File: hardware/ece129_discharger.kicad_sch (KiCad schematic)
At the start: 0 parts

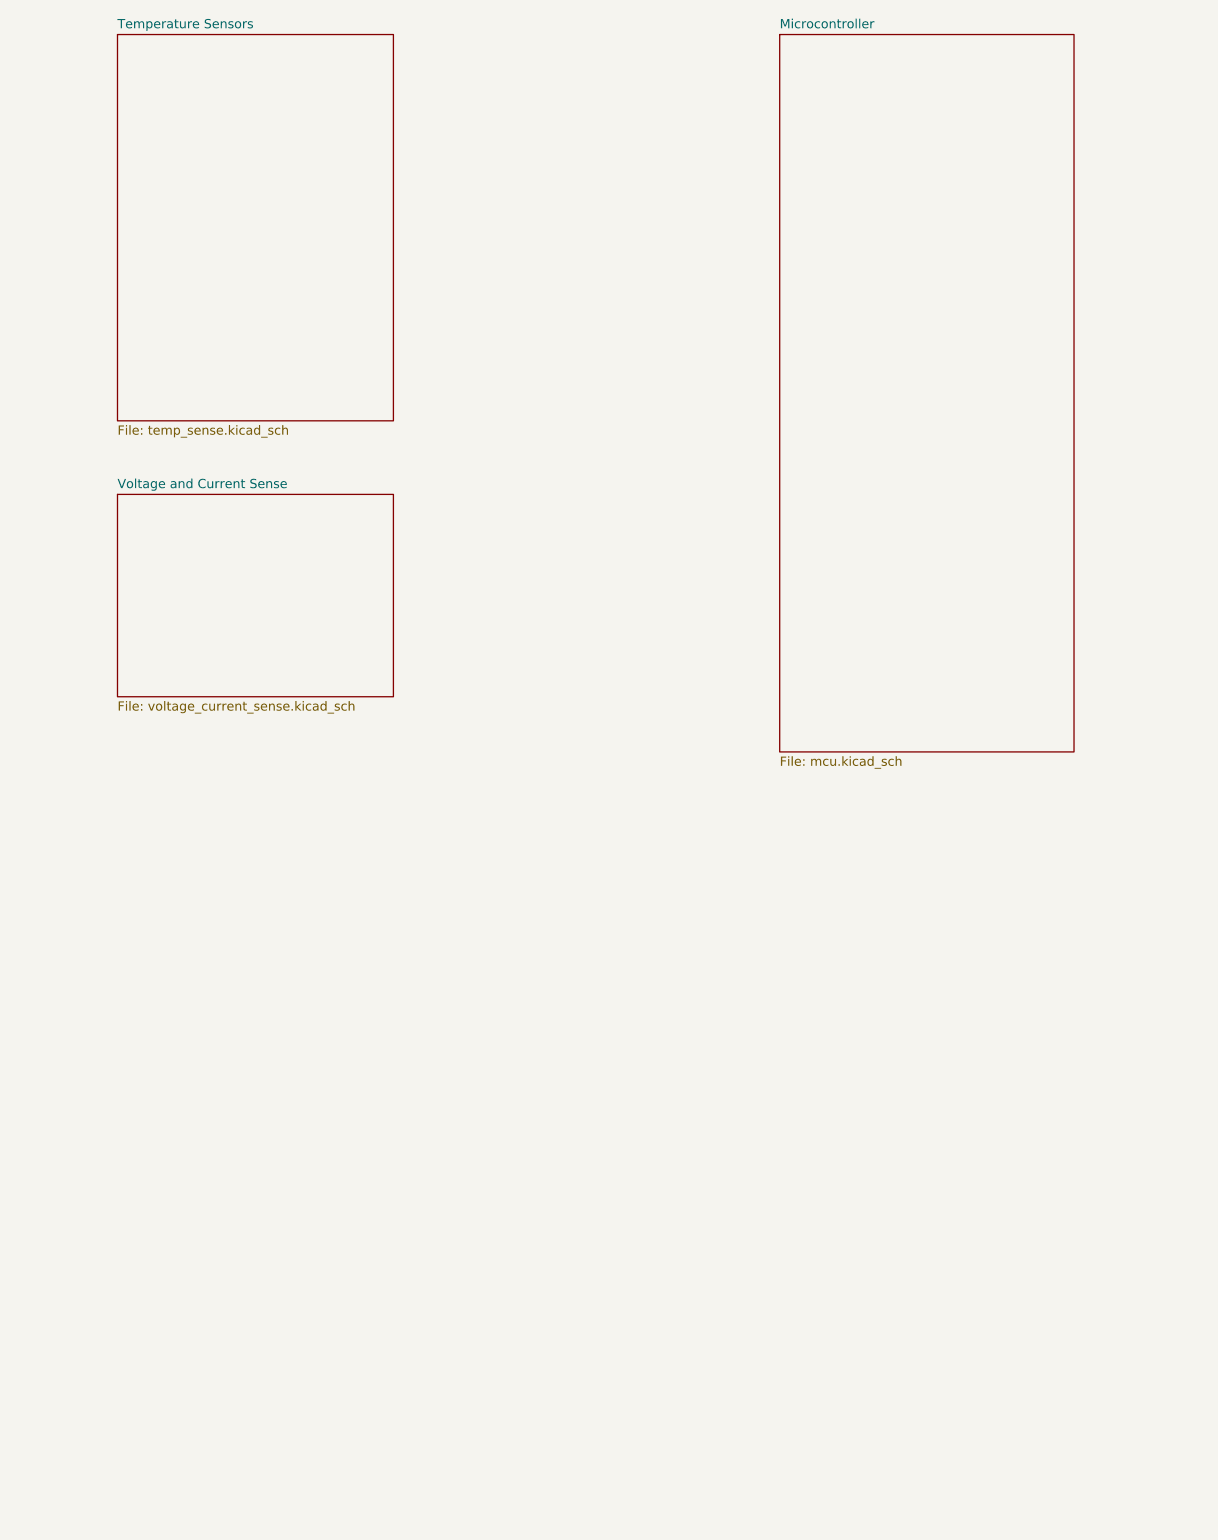
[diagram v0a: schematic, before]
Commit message: MBR0.0.1 - Begin addition of sheet pins to MCU page
Incomplete
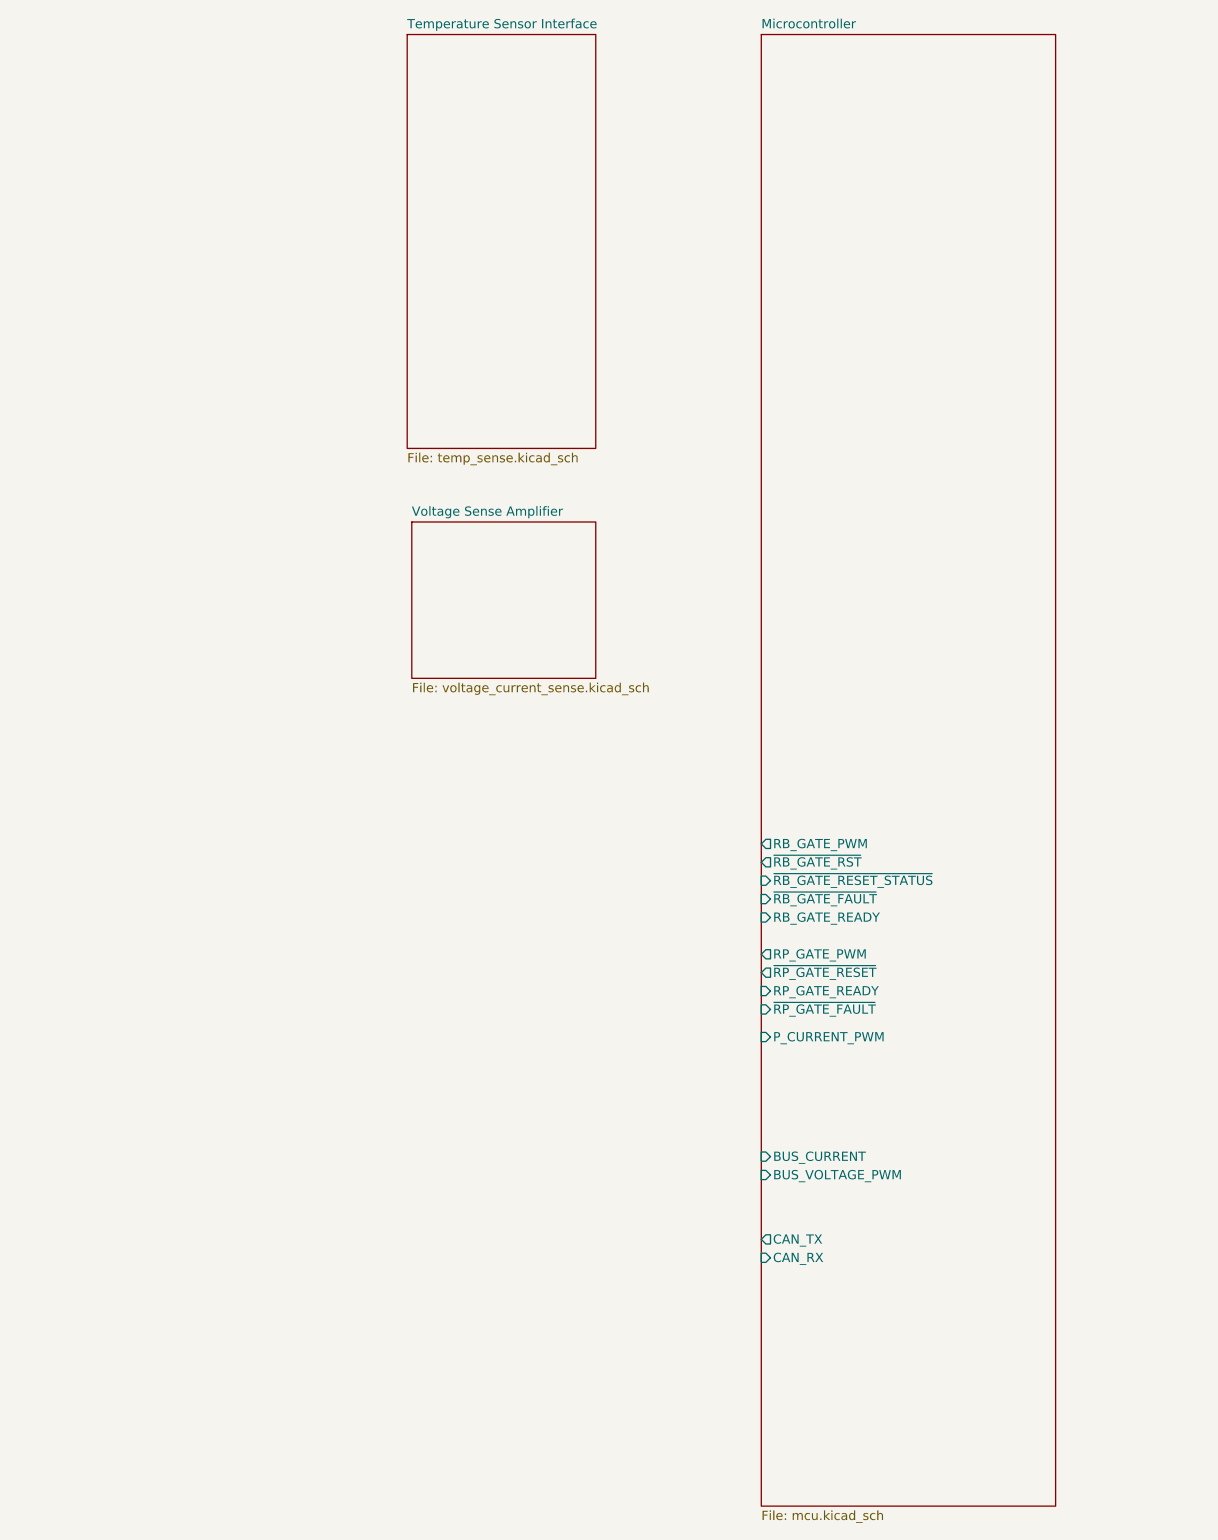
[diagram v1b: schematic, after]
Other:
- sheet Temperature Sensors renamed Temperature Sensor Interface
- sheet Voltage and Current Sense renamed Voltage Sense Amplifier
- sheet Microcontroller ports: added BUS_CURRENT, BUS_VOLTAGE_PWM, CAN_RX, CAN_TX, P_CURRENT_PWM, RB_GATE_PWM, RB_GATE_READY, RP_GATE_PWM, RP_GATE_READY, ~{RB_GATE_FAULT}, ~{RB_GATE_RESET_STATUS}, ~{RB_GATE_RST}, ~{RP_GATE_FAULT}, ~{RP_GATE_RESET}; removed none
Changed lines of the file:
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@@
 	)
 	(sheet
-		(at 152.4 50.8)
-		(size 40.64 99.06)
+		(at 149.86 50.8)
+		(size 40.64 203.2)
 		(exclude_from_sim no)
 		(in_bom yes)
@@
 		)
 		(property "Sheetname" "Microcontroller"
-			(at 152.4 50.0884 0)
+			(at 149.86 50.0884 0)
 			(show_name no)
 			(do_not_autoplace no)
@@
 		)
 		(property "Sheetfile" "mcu.kicad_sch"
-			(at 152.4 150.4446 0)
+			(at 149.86 254.5846 0)
 			(show_name no)
 			(do_not_autoplace no)
@@
 				)
 				(justify left top)
+			)
+		)
+		(pin "~{RB_GATE_RST}" output
+			(at 149.86 165.1 180)
+			(effects
+				(font
+					(size 1.27 1.27)
+				)
+				(justify left)
+			)
+		)
+		(pin "~{RB_GATE_FAULT}" input
+			(at 149.86 170.18 180)
+			(effects
+				(font
+					(size 1.27 1.27)
+				)
+				(justify left)
+			)
+		)
+		(pin "RB_GATE_READY" input
+			(at 149.86 172.72 180)
+			(effects
+				(font
+					(size 1.27 1.27)
+				)
+				(justify left)
+			)
+		)
+		(pin "~{RB_GATE_RESET_STATUS}" input
+			(at 149.86 167.64 180)
+			(effects
+				(font
+					(size 1.27 1.27)
+				)
+				(justify left)
+			)
+		)
+		(pin "RB_GATE_PWM" output
+			(at 149.86 162.56 180)
+			(effects
+				(font
+					(size 1.27 1.27)
+				)
+				(justify left)
+			)
+		)
+		(pin "RP_GATE_PWM" output
+			(at 149.86 177.8 180)
+			(effects
+				(font
+					(size 1.27 1.27)
+				)
+				(justify left)
+			)
+		)
+		(pin "RP_GATE_READY" input
+			(at 149.86 182.88 180)
+			(effects
+				(font
+					(size 1.27 1.27)
+				)
+				(justify left)
+			)
+		)
+		(pin "~{RP_GATE_RESET}" output
+			(at 149.86 180.34 180)
+			(effects
+				(font
+					(size 1.27 1.27)
+				)
+				(justify left)
+			)
+		)
+		(pin "~{RP_GATE_FAULT}" input
+			(at 149.86 185.42 180)
+			(effects
+				(font
+					(size 1.27 1.27)
+				)
+				(justify left)
+			)
+		)
+		(pin "BUS_CURRENT" input
+			(at 149.86 205.74 180)
+			(effects
+				(font
+					(size 1.27 1.27)
+				)
+				(justify left)
+			)
+		)
+		(pin "BUS_VOLTAGE_PWM" input
+			(at 149.86 208.28 180)
+			(effects
+				(font
+					(size 1.27 1.27)
+				)
+				(justify left)
+			)
+		)
+		(pin "CAN_RX" input
+			(at 149.86 219.71 180)
+			(effects
+				(font
+					(size 1.27 1.27)
+				)
+				(justify left)
+			)
+		)
+		(pin "CAN_TX" output
+			(at 149.86 217.17 180)
+			(effects
+				(font
+					(size 1.27 1.27)
+				)
+				(justify left)
+			)
+		)
+		(pin "P_CURRENT_PWM" input
+			(at 149.86 189.23 180)
+			(effects
+				(font
+					(size 1.27 1.27)
+				)
+				(justify left)
 			)
 		)
@@
 	)
 	(sheet
-		(at 60.96 50.8)
-		(size 38.1 53.34)
+		(at 100.965 50.8)
+		(size 26.035 57.15)
 		(exclude_from_sim no)
 		(in_bom yes)
@@
 			(color 0 0 0 0)
 		)
-		(property "Sheetname" "Temperature Sensors"
-			(at 60.96 50.0884 0)
+		(property "Sheetname" "Temperature Sensor Interface"
+			(at 100.965 50.0884 0)
 			(show_name no)
 			(do_not_autoplace no)
@@
 		)
 		(property "Sheetfile" "temp_sense.kicad_sch"
-			(at 60.96 104.7246 0)
+			(at 100.965 108.5346 0)
 			(show_name no)
 			(do_not_autoplace no)
@@
 	)
 	(sheet
-		(at 60.96 114.3)
-		(size 38.1 27.94)
+		(at 101.6 118.11)
+		(size 25.4 21.59)
 		(exclude_from_sim no)
 		(in_bom yes)
@@
 			(color 0 0 0 0)
 		)
-		(property "Sheetname" "Voltage and Current Sense"
-			(at 60.96 113.5884 0)
+		(property "Sheetname" "Voltage Sense Amplifier"
+			(at 101.6 117.3984 0)
 			(show_name no)
 			(do_not_autoplace no)
@@
 		)
 		(property "Sheetfile" "voltage_current_sense.kicad_sch"
-			(at 60.96 142.8246 0)
-			(show_name no)
-			(do_not_autoplace no)
+			(at 101.6 140.2846 0)
+			(show_name no)
+			(do_not_autoplace no)

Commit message: R0.0.2 Add more connections to MCU, some connectors
commit d1f92fde9a9b01f608e388bb27e003f4547c4ba5
Author: fezboy <31973884+fezboy@users.noreply.github.com>
Date:   Tue Apr 28 12:29:51 2026 -0700

    R0.0.2 Add more connections to MCU, some connectors
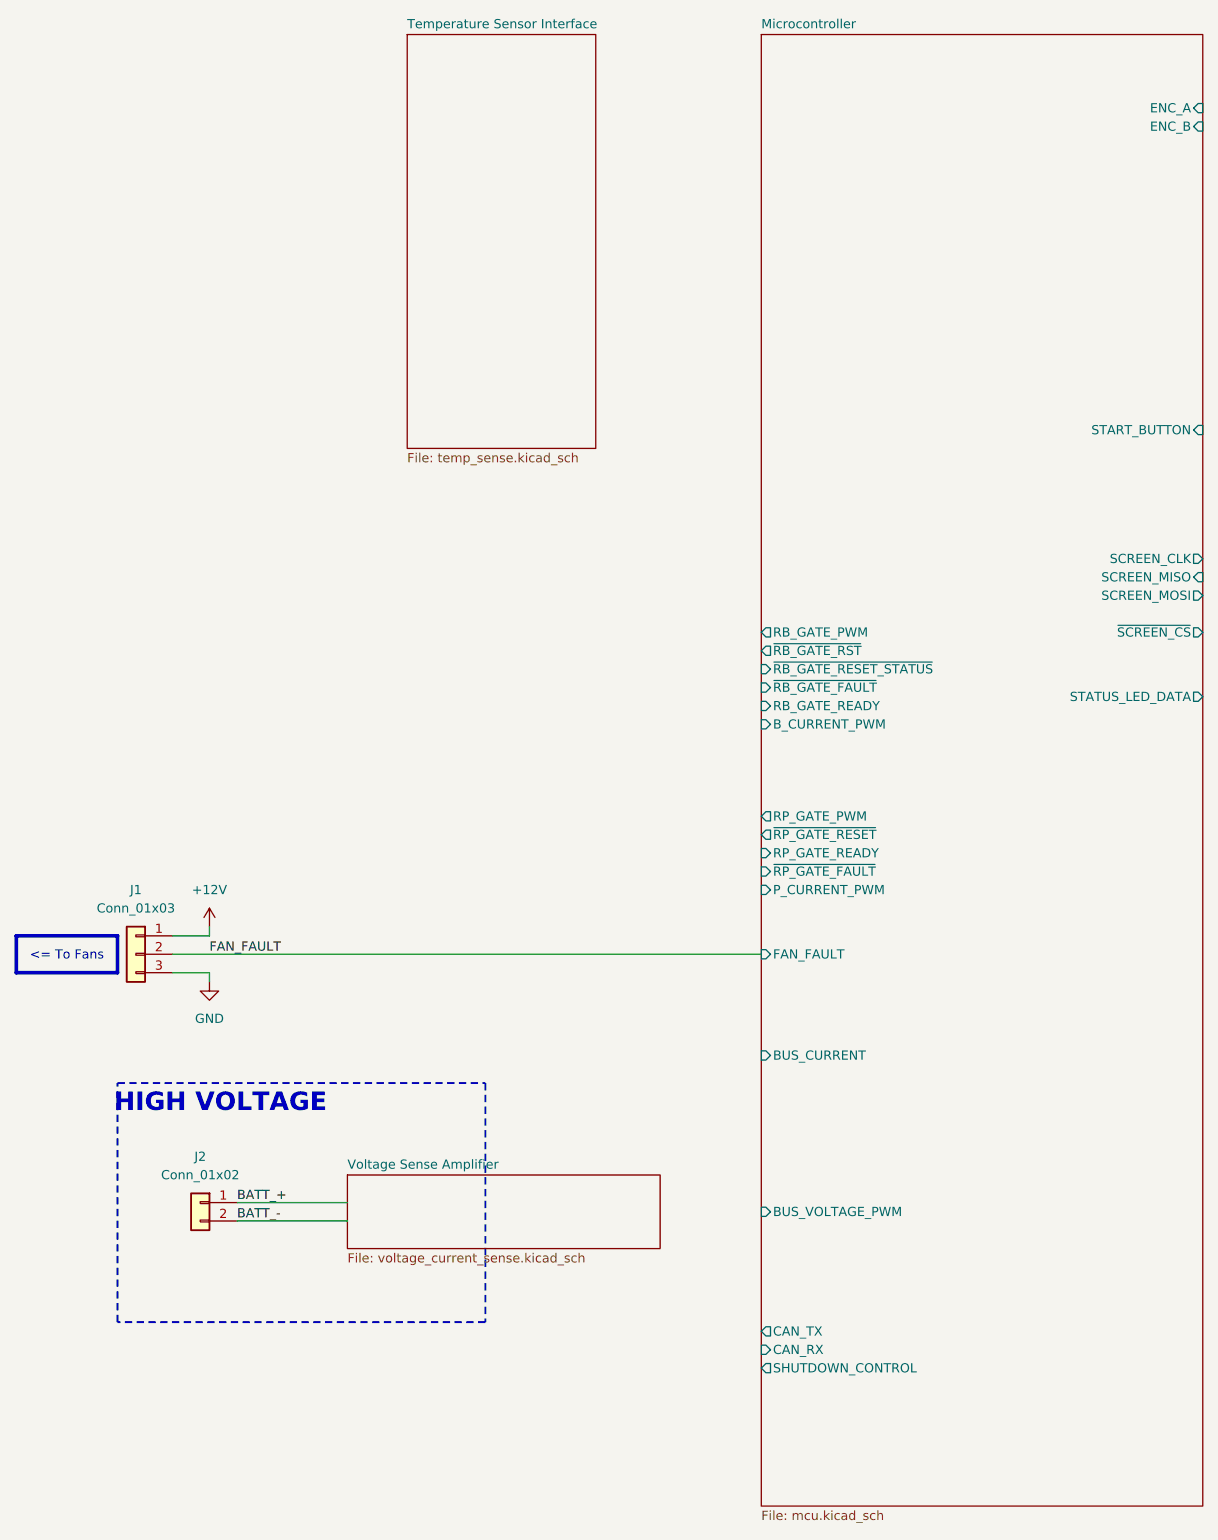
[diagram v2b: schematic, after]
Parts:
- added J1: Conn_01x03, symbol Connector_Generic:Conn_01x03
- added J2: Conn_01x02, symbol Connector_Generic:Conn_01x02
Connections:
- new net +12V: J1.1 (Pin_1)
- new net BATT_+: J2.1 (Pin_1)
- new net BATT_-: J2.2 (Pin_2)
- new net FAN_FAULT: J1.2 (Pin_2)
- new net GND: J1.3 (Pin_3)
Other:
- sheet Microcontroller ports: added B_CURRENT_PWM, ENC_A, ENC_B, FAN_FAULT, SCREEN_CLK, SCREEN_MISO, SCREEN_MOSI, SHUTDOWN_CONTROL, START_BUTTON, STATUS_LED_DATA, ~{SCREEN_CS}; removed none
- note added: "HIGH VOLTAGE"
- title: [BOARD NAME] -> Discharger Main Board

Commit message: adding connectors
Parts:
- added J10, J11, J3, J4, J5, J6, J7, J8, J9: Conn_01x02, symbol Connector_Generic:Conn_01x02
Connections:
- new net CurrentSens_Out: J11.1 (Pin_1)
- new net CurrentSens_Vref: J11.2 (Pin_2)
- new net Temp1_1: J3.1 (Pin_1)
- new net Temp1_2: J3.2 (Pin_2)
- new net Temp2_1: J4.1 (Pin_1)
- new net Temp2_2: J4.2 (Pin_2)
- new net Temp3_1: J5.1 (Pin_1)
- new net Temp3_2: J5.2 (Pin_2)
- new net Temp4_1: J6.1 (Pin_1)
- new net Temp4_2: J6.2 (Pin_2)
- new net Temp5_1: J7.1 (Pin_1)
- new net Temp5_2: J7.2 (Pin_2)
- new net Temp6_1: J8.1 (Pin_1)
- new net Temp6_2: J8.2 (Pin_2)
- new net Temp7_1: J9.1 (Pin_1)
- new net Temp7_2: J9.2 (Pin_2)
- new net Temp8_1: J10.1 (Pin_1)
- new net Temp8_2: J10.2 (Pin_2)

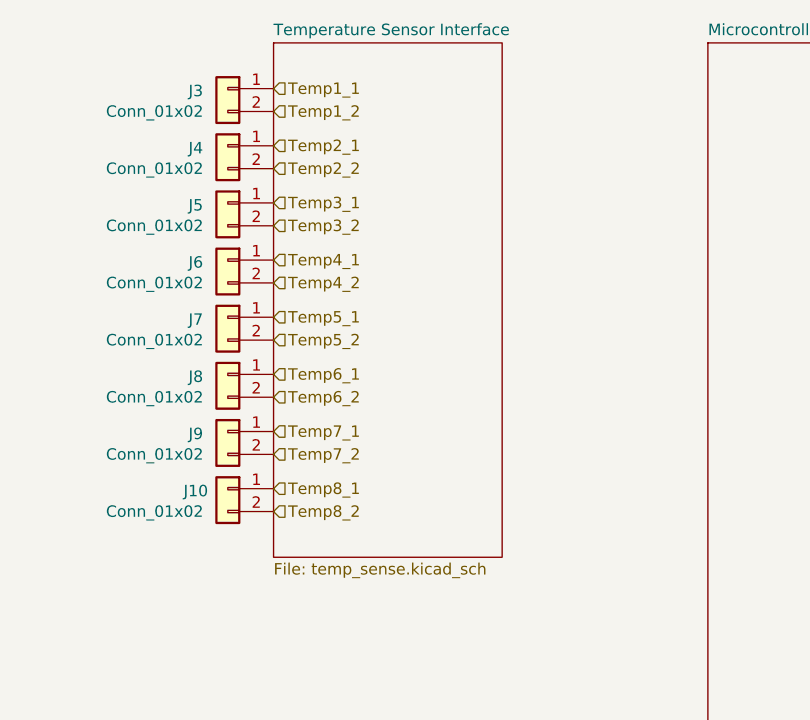
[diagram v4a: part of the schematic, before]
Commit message: Pin assignment first draft
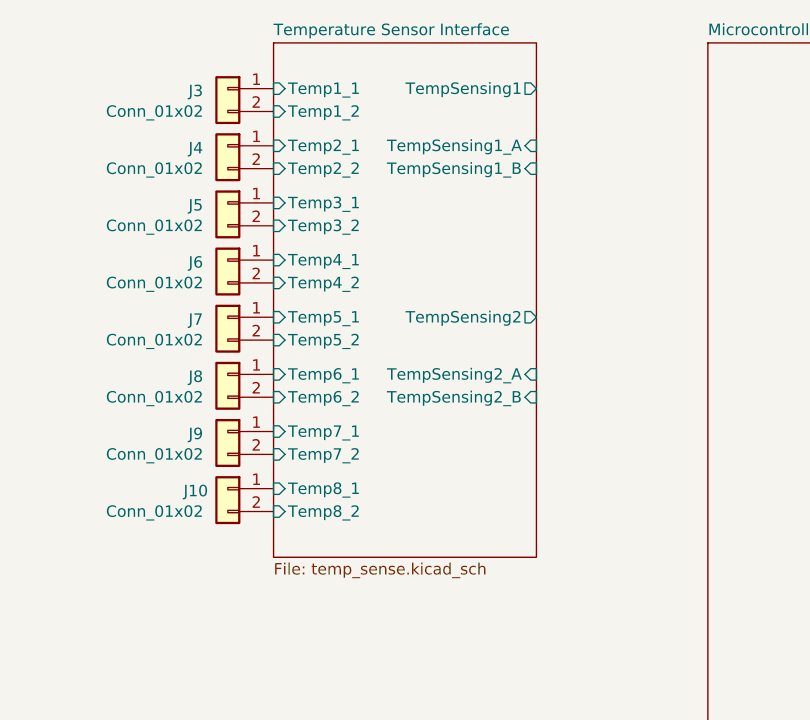
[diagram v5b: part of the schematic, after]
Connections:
- net Temp1_1 renamed Temperature Sensor Interface/Temp1_1
- net Temp1_2 renamed Temperature Sensor Interface/Temp1_2
- net Temp2_1 renamed Temperature Sensor Interface/Temp2_1
- net Temp2_2 renamed Temperature Sensor Interface/Temp2_2
- net Temp3_1 renamed Temperature Sensor Interface/Temp3_1
- net Temp3_2 renamed Temperature Sensor Interface/Temp3_2
- net Temp4_1 renamed Temperature Sensor Interface/Temp4_1
- net Temp4_2 renamed Temperature Sensor Interface/Temp4_2
- net Temp5_1 renamed Temperature Sensor Interface/Temp5_1
- net Temp5_2 renamed Temperature Sensor Interface/Temp5_2
- net Temp6_1 renamed Temperature Sensor Interface/Temp6_1
- net Temp6_2 renamed Temperature Sensor Interface/Temp6_2
- net Temp7_1 renamed Temperature Sensor Interface/Temp7_1
- net Temp7_2 renamed Temperature Sensor Interface/Temp7_2
- net Temp8_1 renamed Temperature Sensor Interface/Temp8_1
- net Temp8_2 renamed Temperature Sensor Interface/Temp8_2
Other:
- sheet Temperature Sensor Interface ports: added Temp1_1, Temp1_2, Temp2_1, Temp2_2, Temp3_1, Temp3_2, Temp4_1, Temp4_2, Temp5_1, Temp5_2, Temp6_1, Temp6_2, Temp7_1, Temp7_2, Temp8_1, Temp8_2, TempSensing1, TempSensing1_A, TempSensing1_B, TempSensing2, TempSensing2_A, TempSensing2_B; removed none
